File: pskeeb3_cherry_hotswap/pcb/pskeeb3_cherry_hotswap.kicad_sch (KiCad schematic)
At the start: 42 parts, among them J2 OLED, K11 KEYSW, K12 KEYSW, K13 KEYSW, K14 KEYSW, K15 KEYSW, K21 KEYSW, K22 KEYSW, K23 KEYSW, K24 KEYSW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

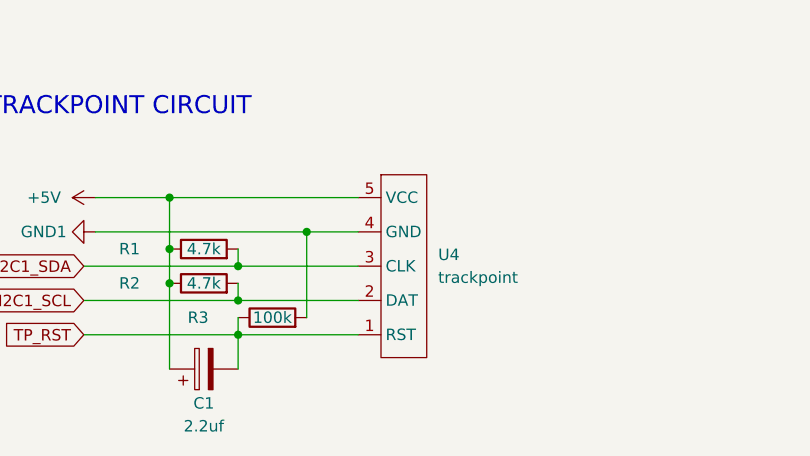
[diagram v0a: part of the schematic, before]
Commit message: feat: added hugebug trackball
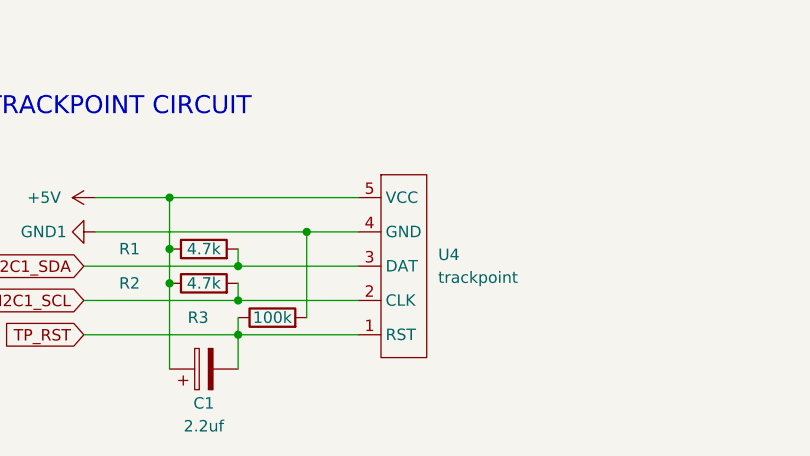
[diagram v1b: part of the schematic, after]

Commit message: refactor: increase footprint pads for easier soldering
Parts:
- C1: footprint Capacitor_SMD:C_1206_3216Metric_Pad1.33x1.80mm_HandSolder -> kwkb-footprint:C_1206_3216Metric_Pad1.33x1.80mm_HandSolder
- LED3: footprint LED_SMD:LED_WS2812B_PLCC4_5.0x5.0mm_P3.2mm -> kwkb-footprint:LED_WS2812B_PLCC4_5.0x5.0mm_P3.2mm
- R1, R2, R3: footprint Resistor_SMD:R_1206_3216Metric_Pad1.30x1.75mm_HandSolder -> kwkb-footprint:R_1206_3216Metric_Pad1.30x1.75mm_HandSolder
- U4: footprint Connector_JST:JST_GH_BM05B-GHS-TBT_1x05-1MP_P1.25mm_Vertical -> kwkb-footprint:JST_GH_BM05B-GHS-TBT_1x05-1MP_P1.25mm_Vertical
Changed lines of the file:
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@@
 			)
 		)
-		(property "Footprint" "Resistor_SMD:R_1206_3216Metric_Pad1.30x1.75mm_HandSolder"
+		(property "Footprint" "kwkb-footprint:R_1206_3216Metric_Pad1.30x1.75mm_HandSolder"
 			(at 118.745 178.943 90)
 			(effects
@@
 			)
 		)
-		(property "Footprint" "LED_SMD:LED_WS2812B_PLCC4_5.0x5.0mm_P3.2mm"
+		(property "Footprint" "kwkb-footprint:LED_WS2812B_PLCC4_5.0x5.0mm_P3.2mm"
 			(at 182.245 57.785 0)
 			(effects
@@
 			)
 		)
-		(property "Footprint" "LED_SMD:LED_WS2812B_PLCC4_5.0x5.0mm_P3.2mm"
+		(property "Footprint" "kwkb-footprint:LED_WS2812B_PLCC4_5.0x5.0mm_P3.2mm"
 			(at 96.52 57.785 0)
 			(effects
@@
 			)
 		)
-		(property "Footprint" "Capacitor_SMD:C_1206_3216Metric_Pad1.33x1.80mm_HandSolder"
+		(property "Footprint" "kwkb-footprint:C_1206_3216Metric_Pad1.33x1.80mm_HandSolder"
 			(at 122.555 185.7248 0)
 			(effects
@@
 			)
 		)
-		(property "Footprint" "LED_SMD:LED_WS2812B_PLCC4_5.0x5.0mm_P3.2mm"
+		(property "Footprint" "kwkb-footprint:LED_WS2812B_PLCC4_5.0x5.0mm_P3.2mm"
 			(at 182.245 36.83 0)
 			(effects
@@
 			)
 		)
-		(property "Footprint" "LED_SMD:LED_WS2812B_PLCC4_5.0x5.0mm_P3.2mm"
+		(property "Footprint" "kwkb-footprint:LED_WS2812B_PLCC4_5.0x5.0mm_P3.2mm"
 			(at 125.73 57.785 0)
 			(effects
@@
 			)
 		)
-		(property "Footprint" "LED_SMD:LED_WS2812B_PLCC4_5.0x5.0mm_P3.2mm"
+		(property "Footprint" "kwkb-footprint:LED_WS2812B_PLCC4_5.0x5.0mm_P3.2mm"
 			(at 96.52 36.83 0)
 			(effects
@@
 			)
 		)
-		(property "Footprint" "LED_SMD:LED_WS2812B_PLCC4_5.0x5.0mm_P3.2mm"
+		(property "Footprint" "kwkb-footprint:LED_WS2812B_PLCC4_5.0x5.0mm_P3.2mm"
 			(at 69.215 36.83 0)
 			(effects
@@
 			)
 		)
-		(property "Footprint" "LED_SMD:LED_WS2812B_PLCC4_5.0x5.0mm_P3.2mm"
+		(property "Footprint" "kwkb-footprint:LED_WS2812B_PLCC4_5.0x5.0mm_P3.2mm"
 			(at 153.035 36.83 0)
 			(effects
@@
 			)
 		)
-		(property "Footprint" "LED_SMD:LED_WS2812B_PLCC4_5.0x5.0mm_P3.2mm"
+		(property "Footprint" "kwkb-footprint:LED_WS2812B_PLCC4_5.0x5.0mm_P3.2mm"
 			(at 153.035 57.785 0)
 			(effects
@@
 			)
 		)
-		(property "Footprint" "LED_SMD:LED_WS2812B_PLCC4_5.0x5.0mm_P3.2mm"
+		(property "Footprint" "kwkb-footprint:LED_WS2812B_PLCC4_5.0x5.0mm_P3.2mm"
 			(at 41.275 57.785 0)
 			(effects
@@
 			)
 		)
-		(property "Footprint" "Connector_JST:JST_GH_BM05B-GHS-TBT_1x05-1MP_P1.25mm_Vertical"
+		(property "Footprint" "kwkb-footprint:JST_GH_BM05B-GHS-TBT_1x05-1MP_P1.25mm_Vertical"
 			(at 135.89 165.1 0)
 			(effects
@@
 			)
 		)
-		(property "Footprint" "LED_SMD:LED_WS2812B_PLCC4_5.0x5.0mm_P3.2mm"
+		(property "Footprint" "kwkb-footprint:LED_WS2812B_PLCC4_5.0x5.0mm_P3.2mm"
 			(at 125.73 36.83 0)
 			(effects
@@
 			)
 		)
-		(property "Footprint" "Resistor_SMD:R_1206_3216Metric_Pad1.30x1.75mm_HandSolder"
+		(property "Footprint" "kwkb-footprint:R_1206_3216Metric_Pad1.30x1.75mm_HandSolder"
 			(at 126.365 182.753 90)
 			(effects
@@
 			)
 		)
-		(property "Footprint" "LED_SMD:LED_WS2812B_PLCC4_5.0x5.0mm_P3.2mm"
+		(property "Footprint" "kwkb-footprint:LED_WS2812B_PLCC4_5.0x5.0mm_P3.2mm"
 			(at 69.215 57.785 0)
 			(effects
@@
 			)
 		)
-		(property "Footprint" "Resistor_SMD:R_1206_3216Metric_Pad1.30x1.75mm_HandSolder"
+		(property "Footprint" "kwkb-footprint:R_1206_3216Metric_Pad1.30x1.75mm_HandSolder"
 			(at 118.745 175.133 90)
 			(effects
@@
 			)
 		)
-		(property "Footprint" "LED_SMD:LED_WS2812B_PLCC4_5.0x5.0mm_P3.2mm"
+		(property "Footprint" "kwkb-footprint:LED_WS2812B_PLCC4_5.0x5.0mm_P3.2mm"
 			(at 41.275 36.83 0)
 			(effects
